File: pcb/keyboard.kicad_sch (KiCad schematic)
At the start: 55 parts, among them J1 USB4510-03-1-A, J4 Battery, Q2 2N7002, SW1 PWR, U1 SRV05-4, U3 BQ24075

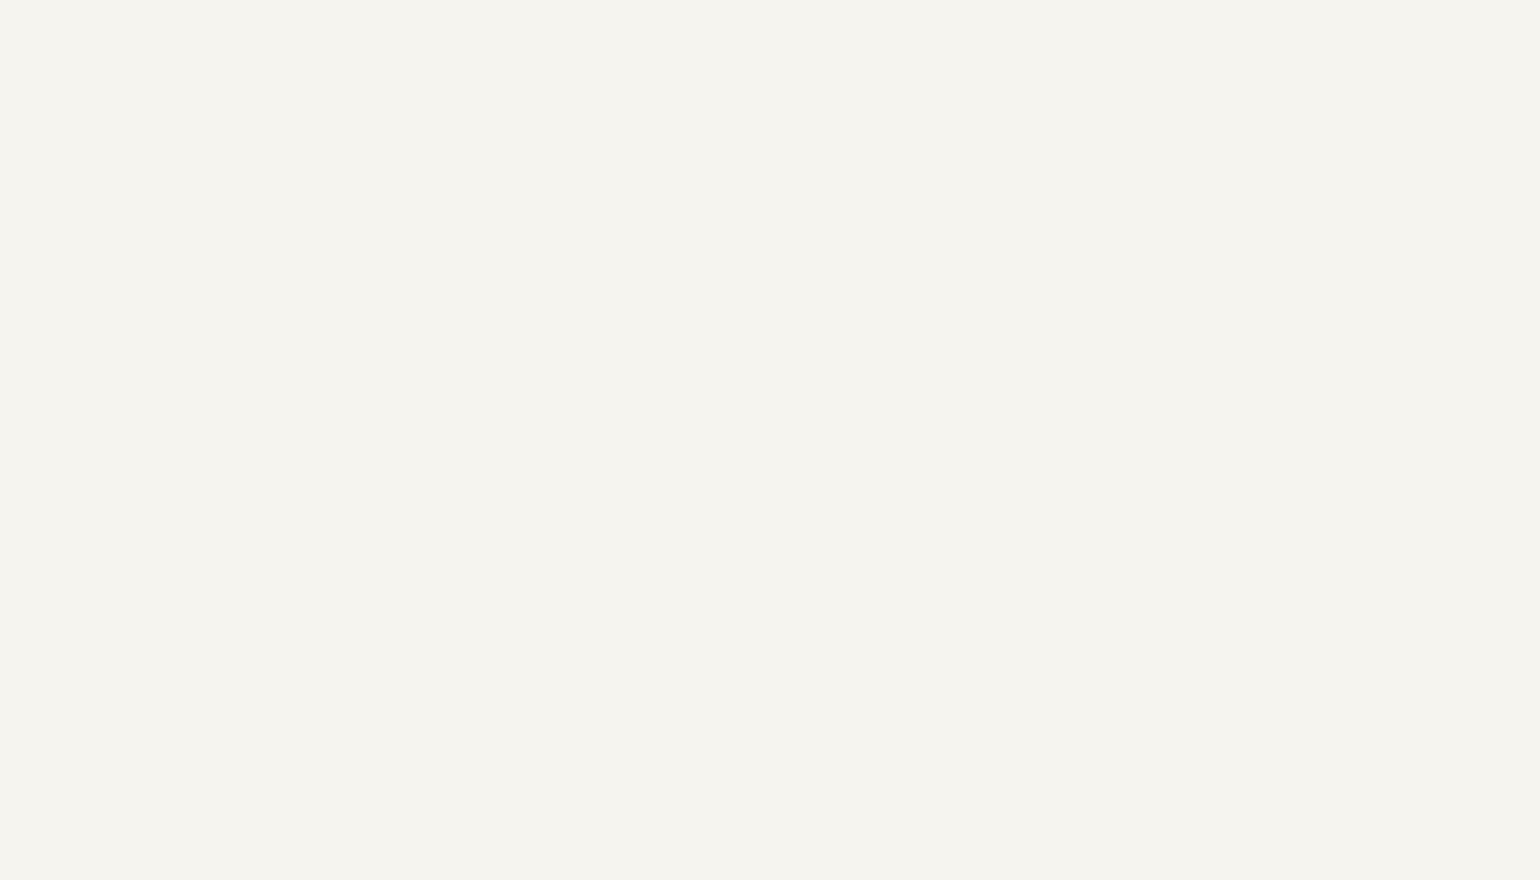
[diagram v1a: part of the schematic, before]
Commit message: #1 add symbol and footprint for BT840
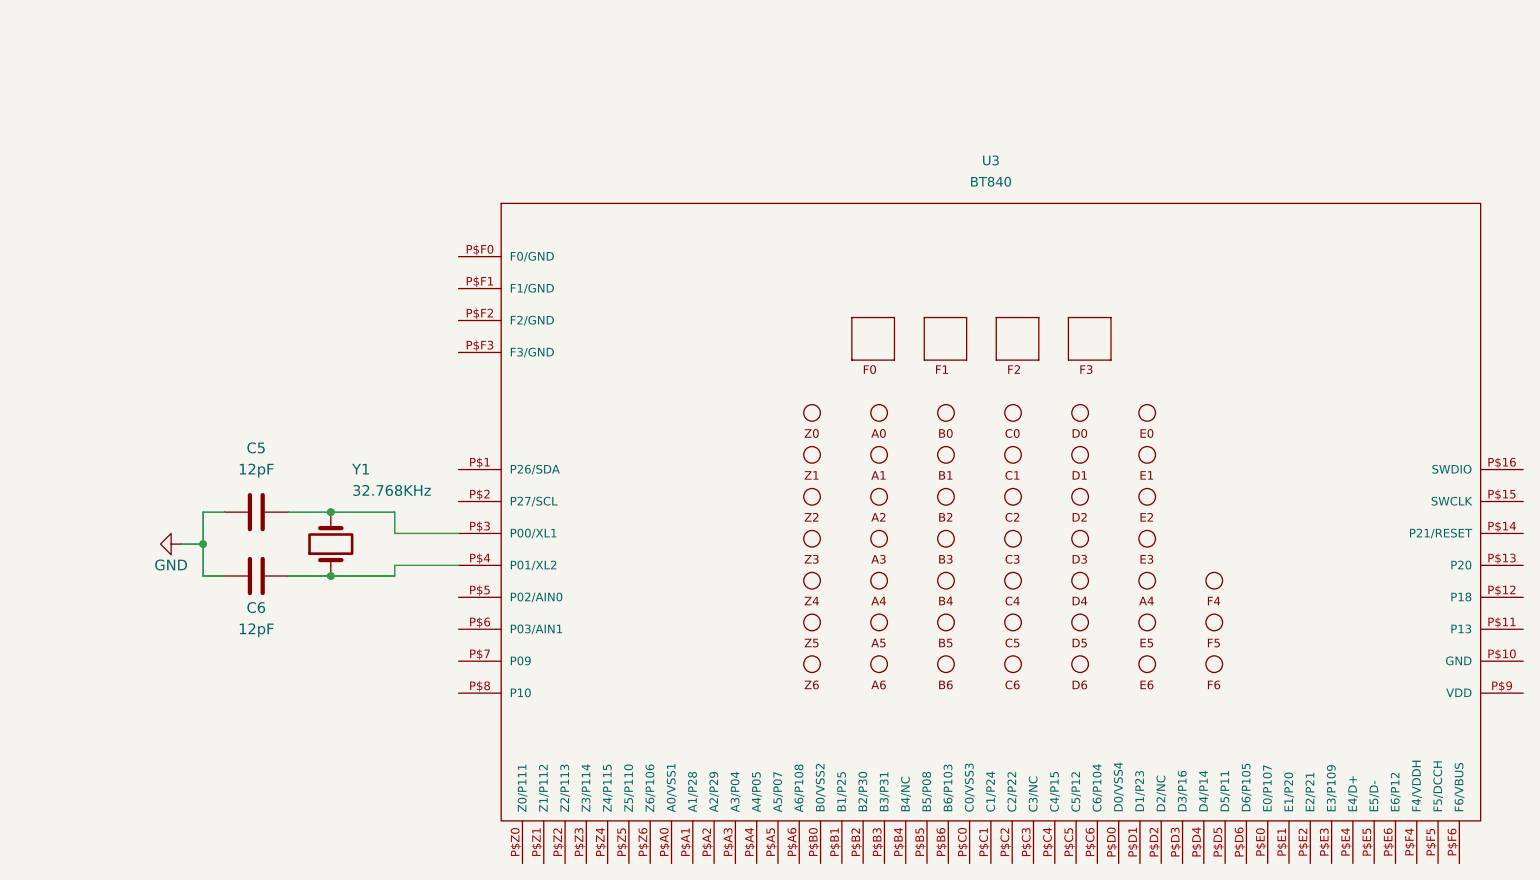
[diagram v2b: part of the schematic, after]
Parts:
- added C5, C6: 12pF, symbol Device:C
- added U3: BT840, BT840_BT840, symbol keyboard:BT840
- added Y1: 32.768KHz, symbol Device:Crystal
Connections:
- net GND: now also C5.1, C6.1
- new net: C6.2, U3.P$4 (P01/XL2), Y1.1
- new net: C5.2, U3.P$3 (P00/XL1), Y1.2
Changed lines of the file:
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@@
   (junction (at 240.03 44.45) (diameter 0) (color 0 0 0 0)
   )
+  (junction (at 212.09 160.02) (diameter 0) (color 0 0 0 0)
+  )
   (junction (at 199.39 69.85) (diameter 0.9144) (color 0 0 0 0)
   )
@@
   (junction (at 275.59 38.1) (diameter 0) (color 0 0 0 0)
   )
+  (junction (at 212.09 167.64) (diameter 0) (color 0 0 0 0)
+  )
   (junction (at 30.48 172.72) (diameter 0.9144) (color 0 0 0 0)
   )
@@
   )
   (junction (at 189.23 69.85) (diameter 0.9144) (color 0 0 0 0)
+  )
+  (junction (at 196.85 163.83) (diameter 0) (color 0 0 0 0)
   )
   (junction (at 186.69 39.37) (diameter 0) (color 0 0 0 0)
@@
     (stroke (width 0) (type default))
   )
+  (wire (pts (xy 194.31 163.83) (xy 196.85 163.83))
+    (stroke (width 0) (type default))
+  )
+  (wire (pts (xy 207.01 167.64) (xy 212.09 167.64))
+    (stroke (width 0) (type default))
+  )
   (polyline (pts (xy 176.53 19.05) (xy 176.53 85.09))
     (stroke (width 0) (type solid))
@@
     (stroke (width 0) (type default))
   )
+  (wire (pts (xy 219.71 166.37) (xy 227.33 166.37))
+    (stroke (width 0) (type default))
+  )
   (wire (pts (xy 275.59 63.5) (xy 280.67 63.5))
     (stroke (width 0) (type default))
   )
+  (wire (pts (xy 219.71 162.56) (xy 227.33 162.56))
+    (stroke (width 0) (type default))
+  )
   (wire (pts (xy 232.41 69.85) (xy 247.65 69.85))
     (stroke (width 0) (type solid))
@@
     (stroke (width 0) (type default))
   )
+  (wire (pts (xy 207.01 160.02) (xy 212.09 160.02))
+    (stroke (width 0) (type default))
+  )
+  (wire (pts (xy 199.39 167.64) (xy 196.85 167.64))
+    (stroke (width 0) (type default))
+  )
   (wire (pts (xy 189.23 69.85) (xy 194.31 69.85))
     (stroke (width 0) (type solid))
@@
     (stroke (width 0) (type solid))
   )
+  (wire (pts (xy 196.85 160.02) (xy 196.85 163.83))
+    (stroke (width 0) (type default))
+  )
   (wire (pts (xy 72.39 140.97) (xy 72.39 138.43))
     (stroke (width 0) (type default))
@@
     (stroke (width 0) (type solid))
   )
+  (wire (pts (xy 196.85 163.83) (xy 196.85 167.64))
+    (stroke (width 0) (type default))
+  )
   (polyline (pts (xy 176.53 19.05) (xy 320.04 19.05))
     (stroke (width 0) (type solid))
@@
     (stroke (width 0) (type default))
   )
+  (wire (pts (xy 212.09 160.02) (xy 219.71 160.02))
+    (stroke (width 0) (type default))
+  )
   (wire (pts (xy 275.59 38.1) (xy 280.67 38.1))
     (stroke (width 0) (type default))
@@
     (stroke (width 0) (type solid))
   )
+  (wire (pts (xy 219.71 160.02) (xy 219.71 162.56))
+    (stroke (width 0) (type default))
+  )
   (wire (pts (xy 228.6 64.77) (xy 240.03 64.77))
     (stroke (width 0) (type solid))
@@
     (stroke (width 0) (type default))
   )
+  (wire (pts (xy 219.71 167.64) (xy 219.71 166.37))
+    (stroke (width 0) (type default))
+  )
   (wire (pts (xy 64.77 133.35) (xy 66.04 133.35))
     (stroke (width 0) (type solid))
@@
   (wire (pts (xy 228.6 52.07) (xy 247.65 52.07))
     (stroke (width 0) (type solid))
+  )
+  (wire (pts (xy 212.09 167.64) (xy 219.71 167.64))
+    (stroke (width 0) (type default))
+  )
+  (wire (pts (xy 196.85 160.02) (xy 199.39 160.02))
+    (stroke (width 0) (type default))
   )
   (wire (pts (xy 38.1 176.53) (xy 38.1 182.88))
@@
     )
   )
+  (symbol (lib_id "Device:C") (at 203.2 167.64 90) (unit 1)
+    (in_bom yes) (on_board yes) (dnp no)
+    (property "Reference" "C6" (at 203.2 171.45 90)
+      (effects (font (size 1.27 1.27)))
+    )
+    (property "Value" "12pF" (at 203.2 173.99 90)
+      (effects (font (size 1.27 1.27)))
+    )
+    (property "Footprint" "" (at 207.01 166.6748 0)
+      (effects (font (size 1.27 1.27)) hide)
+    )
+    (property "Datasheet" "~" (at 203.2 167.64 0)
+      (effects (font (size 1.27 1.27)) hide)
+    )
+    (pin "1")
+    (pin "2")
+    (instances
+      (project "keyboard"
+        (path "/cf0c78e1-ddbc-47c3-b3dc-2a4f1ccfd0ad"
+          (reference "C6") (unit 1)
+        )
+      )
+    )
+  )
   (symbol (lib_id "Switch:SW_Push") (at 85.09 49.53 0) (unit 1)
     (in_bom yes) (on_board yes) (dnp no) (fields_autoplaced)
@@
         (path "/cf0c78e1-ddbc-47c3-b3dc-2a4f1ccfd0ad"
           (reference "S17") (unit 1)
+        )
+      )
+    )
+  )
+  (symbol (lib_id "Device:C") (at 203.2 160.02 90) (unit 1)
+    (in_bom yes) (on_board yes) (dnp no) (fields_autoplaced)
+    (property "Reference" "C5" (at 203.2 152.4 90)
+      (effects (font (size 1.27 1.27)))
+    )
+    (property "Value" "12pF" (at 203.2 154.94 90)
+      (effects (font (size 1.27 1.27)))
+    )
+    (property "Footprint" "" (at 207.01 159.0548 0)
+      (effects (font (size 1.27 1.27)) hide)
+    )
+    (property "Datasheet" "~" (at 203.2 160.02 0)
+      (effects (font (size 1.27 1.27)) hide)
+    )
+    (pin "1")
+    (pin "2")
+    (instances
+      (project "keyboard"
+        (path "/cf0c78e1-ddbc-47c3-b3dc-2a4f1ccfd0ad"
+          (reference "C5") (unit 1)
         )
       )
@@
     )
   )
+  (symbol (lib_id "Device:Crystal") (at 212.09 163.83 90) (unit 1)
+    (in_bom yes) (on_board yes) (dnp no)
+    (property "Reference" "Y1" (at 214.63 154.94 90)
+      (effects (font (size 1.27 1.27)) (justify right))
+    )
+    (property "Value" "32.768KHz" (at 214.63 157.48 90)
+      (effects (font (size 1.27 1.27)) (justify right))
+    )
+    (property "Footprint" "" (at 212.09 163.83 0)
+      (effects (font (size 1.27 1.27)) hide)
+    )
+    (property "Datasheet" "~" (at 212.09 163.83 0)
+      (effects (font (size 1.27 1.27)) hide)
+    )
+    (pin "1")
+    (pin "2")
+    (instances
+      (project "keyboard"
+        (path "/cf0c78e1-ddbc-47c3-b3dc-2a4f1ccfd0ad"
+          (reference "Y1") (unit 1)
+        )
+      )
+    )
+  )
+  (symbol (lib_id "keyboard:BT840") (at 289.56 170.18 0) (unit 1)
+    (in_bom yes) (on_board yes) (dnp no) (fields_autoplaced)
+    (property "Reference" "U3" (at 290.83 118.11 0)
+      (effects (font (size 1.143 1.143)))
+    )
+    (property "Value" "BT840" (at 290.83 120.65 0)
+      (effects (font (size 1.143 1.143)))
+    )
+    (property "Footprint" "BT840_BT840" (at 285.242 166.37 0)
+      (effects (font (size 0.508 0.508)) hide)
+    )
+    (property "Datasheet" "https://static1.squarespace.com/static/561459a2e4b0b39f5cefa12e/t/650e3e75b8b0c6354d09cb72/1695432312154/BT840FN+Product+Specifications.pdf" (at 284.48 170.18 0)
+      (effects (font (size 1.524 1.524)) hide)
+    )
+    (pin "P$E1")
+    (pin "P$F2")
+    (pin "P$D2")
+    (pin "P$B2")
+    (pin "P$B6")
+    (pin "P$B3")
+    (pin "P$C0")
+    (pin "P$C2")
+    (pin "P$9")
+    (pin "P$F3")
+    (pin "P$4")
+    (pin "P$A6")
+    (pin "P$B1")
+    (pin "P$3")
+    (pin "P$1")
+    (pin "P$6")
+    (pin "P$A4")
+    (pin "P$D0")
+    (pin "P$D6")
+    (pin "P$5")
+    (pin "P$Z1")
+    (pin "P$Z6")
+    (pin "P$Z4")
+    (pin "P$8")
+    (pin "P$E3")
+    (pin "P$B0")
+    (pin "P$Z5")
+    (pin "P$F5")
+    (pin "P$D3")
+    (pin "P$C6")
+    (pin "P$A0")
+    (pin "P$F4")
+    (pin "P$F0")
+    (pin "P$E6")
+    (pin "P$7")
+    (pin "P$E5")
+    (pin "P$F1")
+    (pin "P$16")
+    (pin "P$E2")
+    (pin "P$Z3")
+    (pin "P$2")
+    (pin "P$Z0")
+    (pin "P$C1")
+    (pin "P$D5")
+    (pin "P$F6")
+    (pin "P$D1")
+    (pin "P$14")
+    (pin "P$13")
+    (pin "P$A5")
+    (pin "P$C3")
+    (pin "P$Z2")
+    (pin "P$E0")
+    (pin "P$11")
+    (pin "P$C5")
+    (pin "P$15")
+    (pin "P$10")
+    (pin "P$B5")
+    (pin "P$12")
+    (pin "P$E4")
+    (pin "P$B4")
+    (pin "P$D4")
+    (pin "P$A2")
+    (pin "P$A1")
+    (pin "P$A3")
+    (pin "P$C4")
+    (instances
+      (project "keyboard"
+        (path "/cf0c78e1-ddbc-47c3-b3dc-2a4f1ccfd0ad"
+          (reference "U3") (unit 1)
+        )
+      )
+    )
+  )
   (symbol (lib_id "Device:R_Small") (at 275.59 40.64 0) (unit 1)
     (in_bom yes) (on_board yes) (dnp no) (fields_autoplaced)
@@
         )
       )
+    )
+  )
+  (symbol (lib_id "power:GND") (at 194.31 163.83 270) (unit 1)
+    (in_bom yes) (on_board yes) (dnp no)
+    (property "Reference" "#PWR010" (at 187.96 163.83 0)
+      (effects (font (size 1.27 1.27)) hide)
+    )
+    (property "Value" "GND" (at 193.04 166.37 90)
+      (effects (font (size 1.27 1.27)))
+    )
+    (property "Footprint" "" (at 194.31 163.83 0)
+      (effects (font (size 1.27 1.27)) hide)
+    )
+    (property "Datasheet" "" (at 194.31 163.83 0)
+      (effects (font (size 1.27 1.27)) hide)
+    )
+    (pin "1")
+    (instances
+      (project "designguide-schematic"
+        (path "/c2a65ddb-3915-4293-98a9-444287fe2a3d"
+          (reference "#PWR010") (unit 1)
+        )
+      )
+      (project "keyboard"
+        (path "/cf0c78e1-ddbc-47c3-b3dc-2a4f1ccfd0ad"
+          (reference "#PWR021") (unit 1)
+        )
+      )

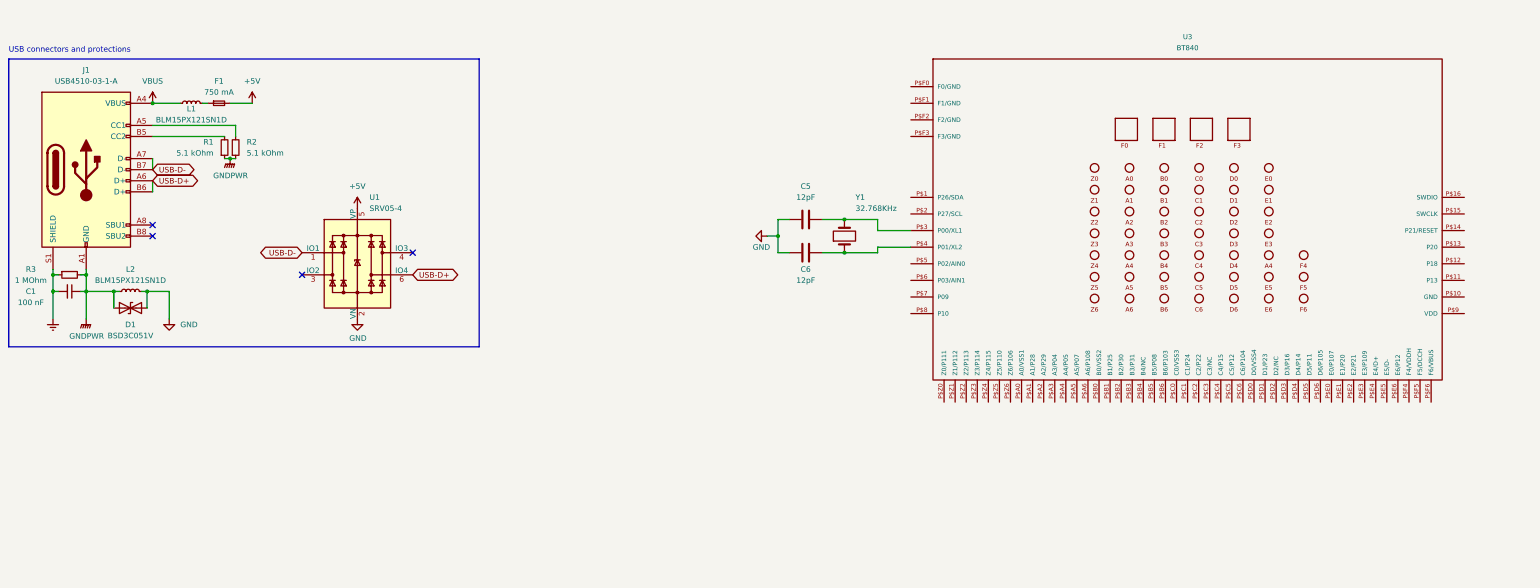
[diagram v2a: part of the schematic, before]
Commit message: #1  fix errors on the  BT840 symbol and footprint
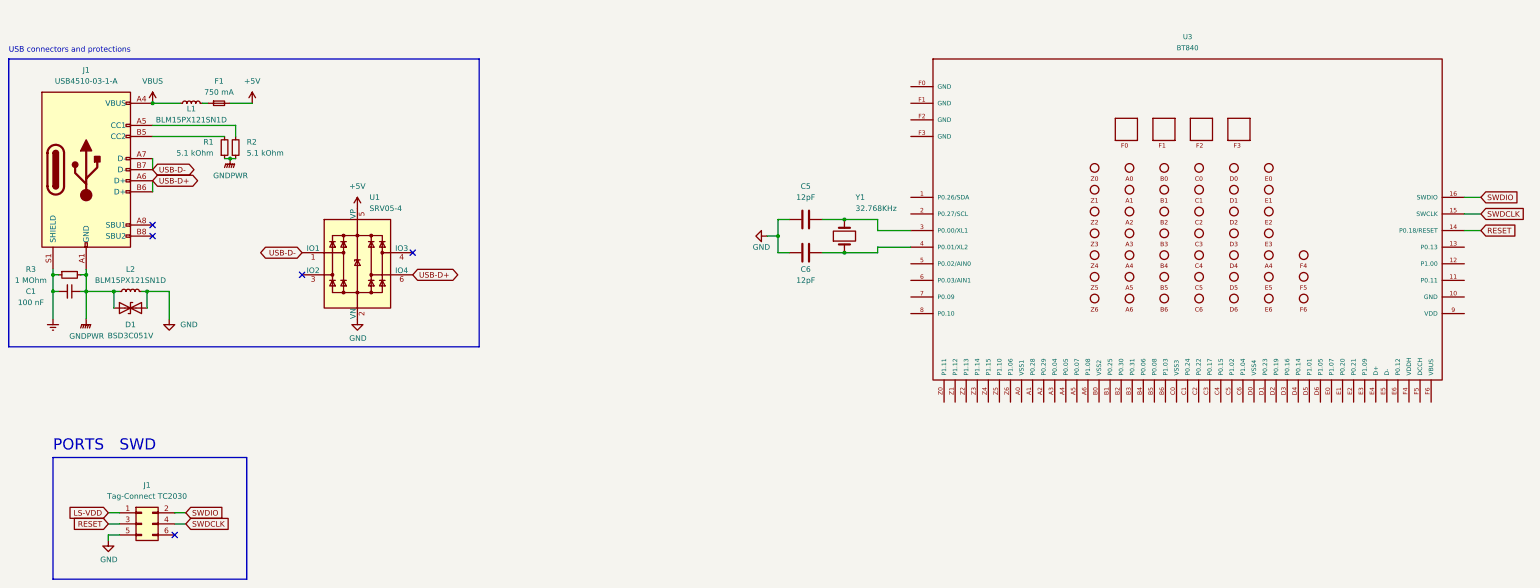
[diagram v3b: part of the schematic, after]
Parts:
- added J1: Tag-Connect TC2030, Connector:Tag-Connect_TC2030-IDC-NL_2x03_P1.27mm_Vertical, symbol Connector_Generic:Conn_02x03_Odd_Even
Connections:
- net GND: now also J1.5 (Pin_5)
- net at C6.2, Y1.1: now also U3.4 (P0.01/XL2); no longer U3.P$4 (P01/XL2)
- net at C5.2, Y1.2: now also U3.3 (P0.00/XL1); no longer U3.P$3 (P00/XL1)
- new net LS-VDD: J1.1 (Pin_1)
- new net RESET: J1.3 (Pin_3), U3.14 (P0.18/RESET)
- new net SWDCLK: J1.4 (Pin_4), U3.15 (SWCLK)
- new net SWDIO: J1.2 (Pin_2), U3.16 (SWDIO)
- no-connect marks 5 -> 6
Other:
- note added: "PORTS"
- note added: "SWD"

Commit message: #1 Add preliminary switch connections on the schematic
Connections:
- net P10 is gone; now on net P0.29: S11.1
- net P11 is gone; now on net P1.13: S12.1
- net P12 is gone; now on net P1.03: S13.1
- net P13 is gone; now on net P0.07: S14.1
- net P14 is gone; now on net P1.14: S15.1
- net P15 is gone; now on net P0.28: S16.1
- net P16 is gone; now on net P1.04: S17.1
- net P17 is gone; now on net P0.08: S18.1
- net P18 is gone; now on net P0.04: S19.1
- net P19 is gone; now on net P0.24: S20.1
- net P2 is gone; now on net P0.27: S3.1
- net P20 is gone; now on net P1.05: S21.1
- net P21 is gone; now on net P1.02: S22.1
- net P22 is gone; now on net P0.20: S23.1
- net P23 is gone; now on net P0.23: S24.1
- net P24 is gone; now on net P0.21: S25.1
- net P25 is gone; now on net P0.12: S26.1
- net P26 is gone; now on net P0.25: S27.1
- net P27 is gone; now on net P1.07: S28.1
- net P28 is gone; now on net P0.21: S29.1
- net P3 is gone; now on net P0.26: S4.1
- net P4 is gone; now on net P1.06: S5.1
- net P5 is gone; now on net P0.05: S6.1
- net P6 is gone; now on net P1.12: S7.1
- net P7 is gone; now on net P1.11: S8.1
- net P8 is gone; now on net P1.08: S9.1
- net P9 is gone; now on net P1.10: S10.1
- net +5V: now also U3.F6 (VBUS)
- net +VSW: now also U3.F4 (VDDH)
- net GND: now also U3.A0 (VSS1), U3.B0 (VSS2), U3.C0 (VSS3), U3.D0 (VSS4), U3.F0 (GND), U3.F1 (GND), U3.F2 (GND), U3.F3 (GND)
- net USB-D+: now also U3.E4 (D+)
- net USB-D-: now also U3.E5 (D-)
- net P0.26: now reaches U3.1 (P0.26/SDA)
- net P0.27: now reaches U3.2 (P0.27/SCL)
- net P0.28: now reaches U3.A1 (P0.28)
- net P0.29: now reaches U3.A2 (P0.29)
- net P0.04: now reaches U3.A3 (P0.04)
- net P0.05: now reaches U3.A4 (P0.05)
- net P0.07: now reaches U3.A5 (P0.07)
- net P1.08: now reaches U3.A6 (P1.08)
- net P0.25: now reaches U3.B1 (P0.25)
- net P0.08: now reaches U3.B5 (P0.08)
- net P1.03: now reaches U3.B6 (P1.03)
- net P0.24: now reaches U3.C1 (P0.24)
- net P1.02: now reaches U3.C5 (P1.02)
- net P1.04: now reaches U3.C6 (P1.04)
- net P0.23: now reaches U3.D1 (P0.23)
- net P1.01: now reaches U3.D5 (P1.01)
- net P1.05: now reaches U3.D6 (P1.05)
- net P1.07: now reaches U3.E0 (P1.07)
- net P0.20: now reaches U3.E1 (P0.20)
- net P0.21: now reaches U3.E2 (P0.21)
- net P1.09: now reaches U3.E3 (P1.09)
- net P0.12: now reaches U3.E6 (P0.12)
- net P1.11: now reaches U3.Z0 (P1.11)
- net P1.12: now reaches U3.Z1 (P1.12)
- net P1.13: now reaches U3.Z2 (P1.13)
- net P1.14: now reaches U3.Z3 (P1.14)
- net P1.15: now reaches U3.Z4 (P1.15)
- net P1.10: now reaches U3.Z5 (P1.10)
- net P1.06: now reaches U3.Z6 (P1.06)
- net P0: no longer names the net of S1.1
- net P1: no longer names the net of S2.1
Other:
- moved on the sheet: C1, C5, C6, C7, D1, F1, J1, J4, L1, L2, LED2, Q2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
